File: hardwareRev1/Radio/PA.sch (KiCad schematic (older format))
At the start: 26 parts

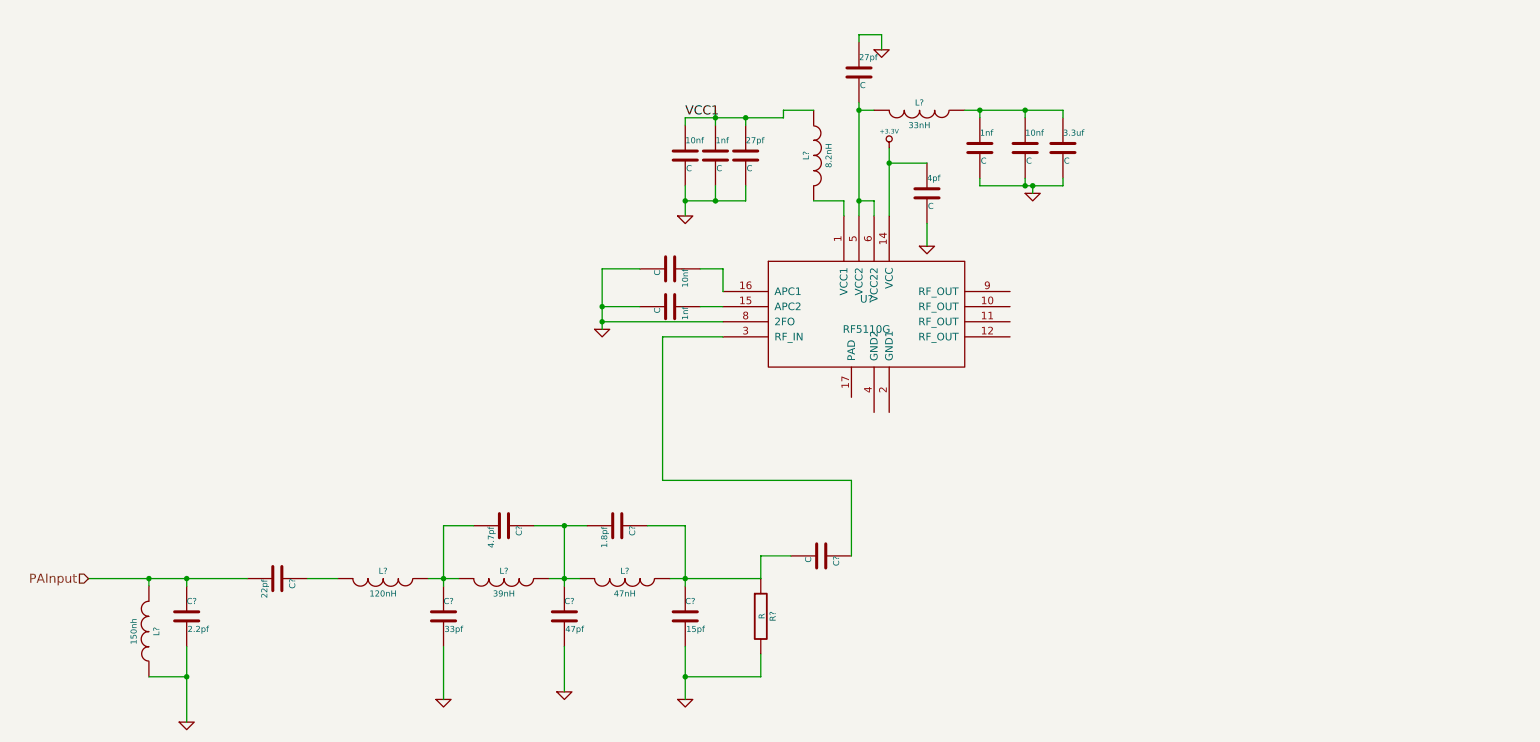
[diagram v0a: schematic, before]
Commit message: Added the outline for the RF module. Also finished the schematic.
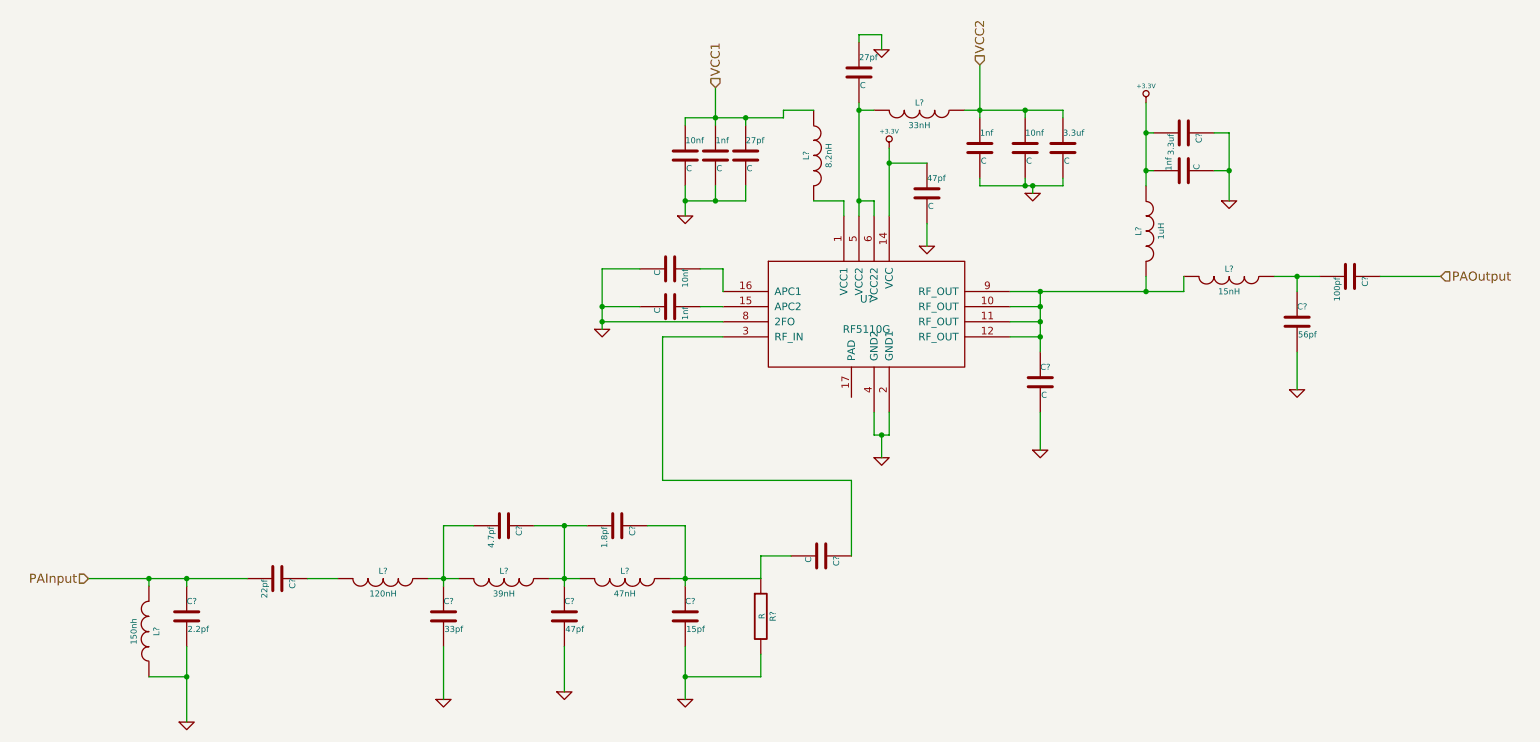
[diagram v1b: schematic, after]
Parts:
- added 1nf, C?: C, symbol C
- added C?: 3.3uf, symbol C
- added C?: 56pf, symbol C
- added C?: 100pf, symbol C
- added L?: 1uH, symbol INDUCTOR
- added L?: 15nH, symbol INDUCTOR
- renumbered 4pf to 47pf
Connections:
- net +3.3V: now also 1nf.1, C?.2, L?.1
- net GND: now also U?.2 (GND1), U?.4 (GND2), 1nf.2, C?.1, C?.2, C?.2
- net at U?.10 (RF_OUT): now also U?.11 (RF_OUT), U?.12 (RF_OUT), U?.9 (RF_OUT), C?.1, L?.2, L?.2
- net VCC2: now reaches 10nf.1, 1nf.1, 3.3uf.1, L?.1
- new net: C?.1, C?.2, L?.1
- new net PAOutput: C?.1

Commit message: added the radio .
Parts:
- C11, C12, C13, C14, C15, C16, C20, C23, C28, C32, C33: renamed from C?; footprint (none) -> Capacitors_SMD:C_0402
- C17, C19, C27: renamed from 10nf; value C -> 10nf; footprint (none) -> Capacitors_SMD:C_0402
- C18, C21, C26, C31: renamed from 1nf; value C -> 1nf; footprint (none) -> Capacitors_SMD:C_0402
- C22, C24: renamed from 27pf; value C -> 27pf; footprint (none) -> Capacitors_SMD:C_0402
- C25: renamed from 47pf; value C -> 47pf; footprint (none) -> Capacitors_SMD:C_0402
- C29: renamed from 3.3uf; value C -> 3.3uf; footprint (none) -> Capacitors_SMD:C_1206
- C30: renamed from C?; footprint (none) -> Capacitors_SMD:C_1206
- L10, L11, L12, L14, L15, L8, L9: renamed from L?; footprint (none) -> Resistors_SMD:R_0402
- L13: renamed from L?; footprint (none) -> Resistors_SMD:R_1206
- R1: renamed from R?; footprint (none) -> Resistors_SMD:R_0402
- U3: renamed from U?; footprint MODULE -> w_smd_qfn:qfn-16
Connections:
- net GND: now also U3.17 (PAD)

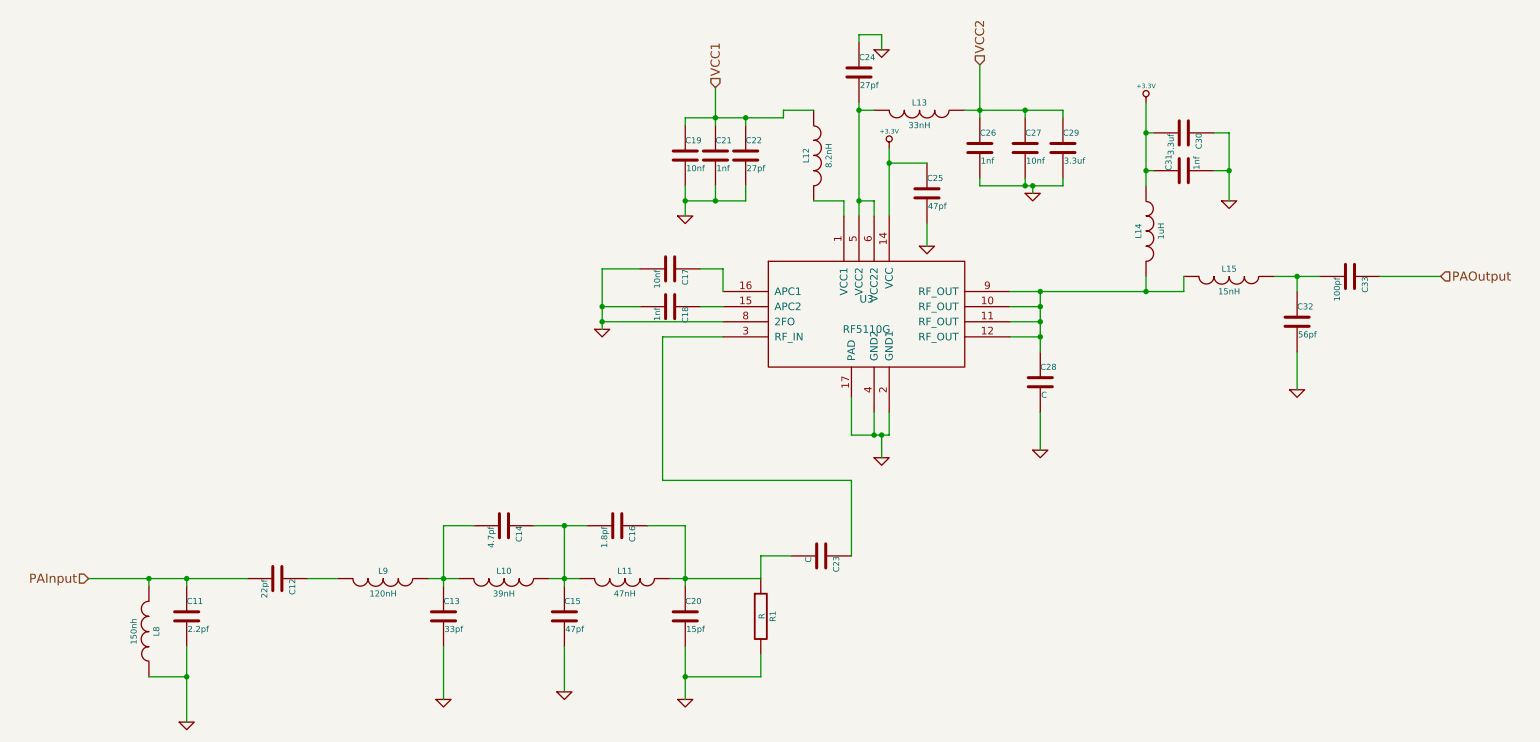
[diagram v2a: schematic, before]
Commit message: Finished the PCB for the new radio module.
Still needs to be checked.
Added the datasheet for the amp and switch
Added the footprint for a 1.27mm pitch 2X8 connector
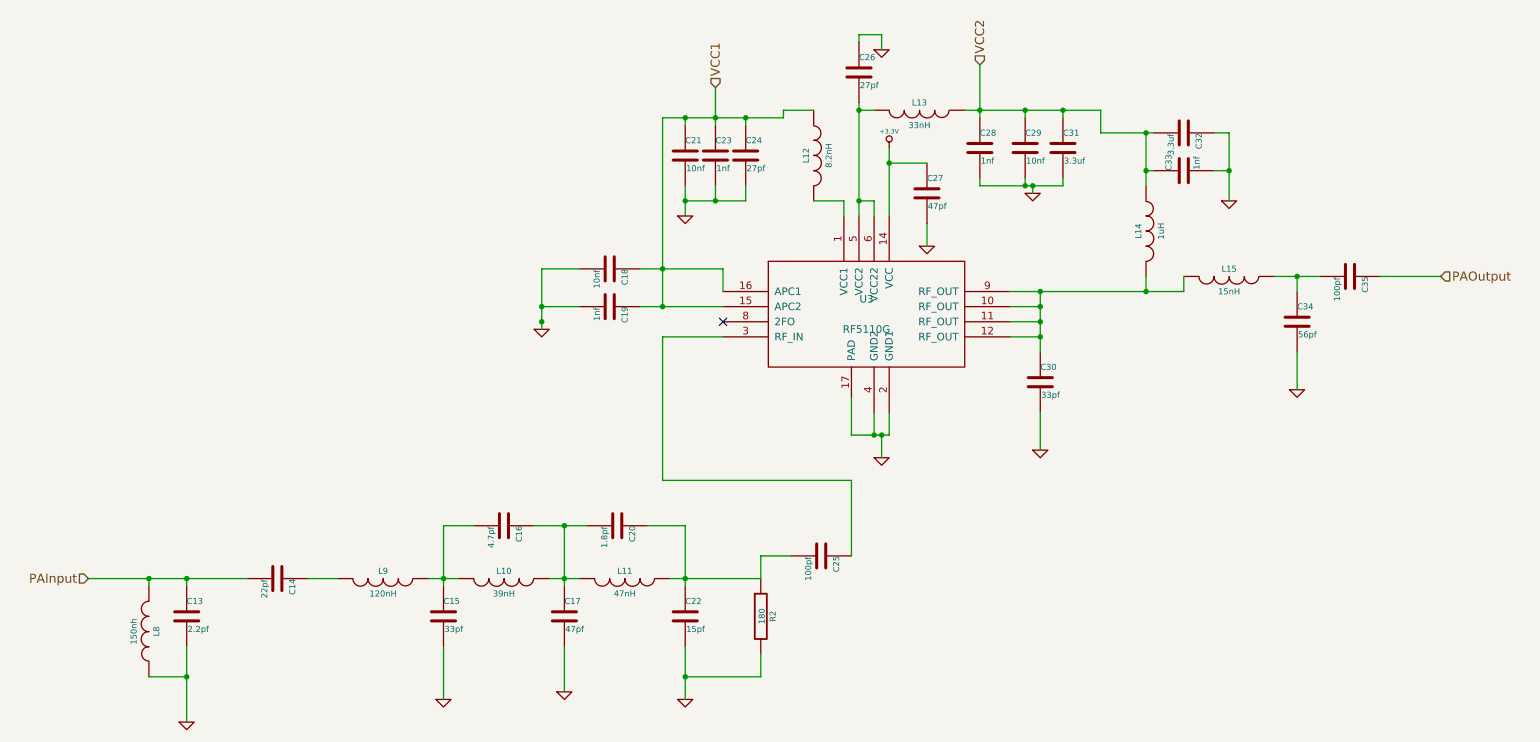
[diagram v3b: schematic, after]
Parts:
- C25: renamed from C23; value C -> 100pf
- C30: renamed from C28; value C -> 33pf
- R2: renamed from R1; value R -> 180
- U3: footprint w_smd_qfn:qfn-16 -> Housings_DFN_QFN:QFN-16-1EP_3x3mm_Pitch0.5mm
- renumbered C11 to C13, C12 to C14, C13 to C15, C14 to C16, C15 to C17, C17 to C18, C18 to C19, C16 to C20, C19 to C21, C20 to C22, C21 to C23, C22 to C24, C24 to C26, C25 to C27, C26 to C28, C27 to C29, C29 to C31, C30 to C32, C31 to C33, C32 to C34, C33 to C35
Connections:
- net +3.3V: no longer C32.2, C33.1, L14.1
- net GND: no longer U3.8 (2FO)
- net VCC1: now also C18.1, C19.1, U3.15 (APC2), U3.16 (APC1)
- net VCC2: now also C32.2, C33.1, L14.1
- no-connect marks 0 -> 1
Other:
- moved on the sheet: C18, C19

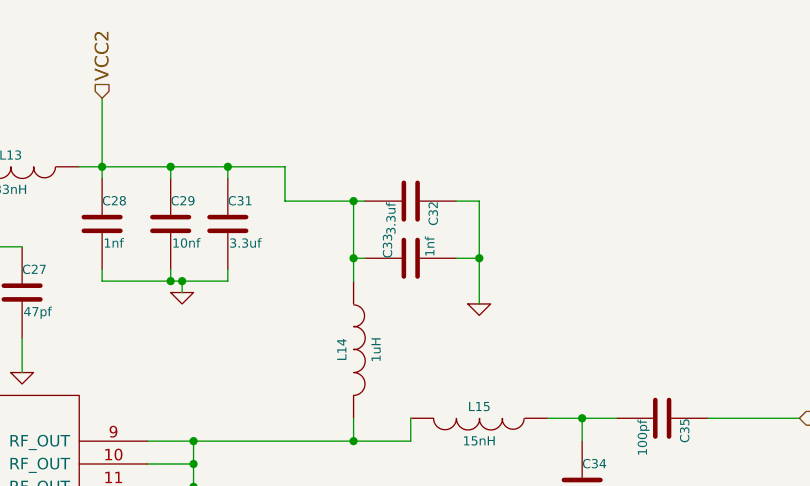
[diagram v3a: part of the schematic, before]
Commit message: Added a capacitor to the power amp sheet in order to facilitate 440.
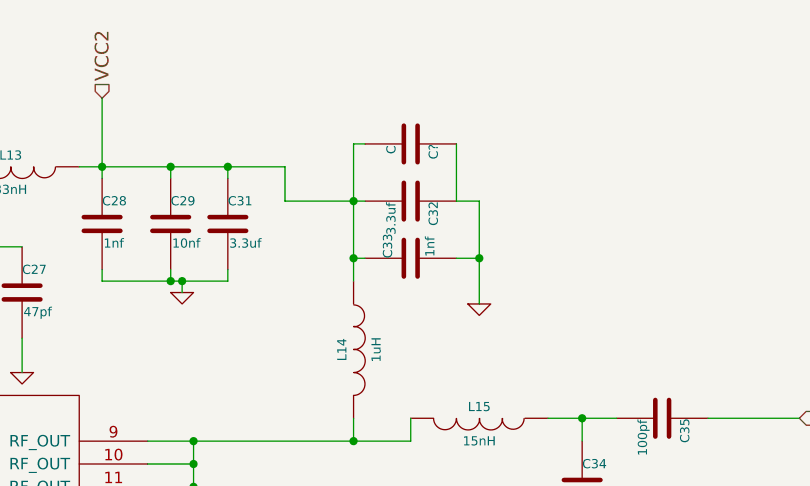
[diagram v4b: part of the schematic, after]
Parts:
- added C?: C, symbol C
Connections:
- net GND: now also C?.1
- net VCC2: now also C?.2
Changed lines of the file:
@@
 Connection ~ 7450 2850
 Wire Wire Line
-	8000 3000 8000 3350
+	8000 2750 8000 3350
 NoConn ~ 5200 4250
+$Comp
+L C C?
+U 1 1 55F187F6
+P 8250 2750
+F 0 "C?" H 8250 2850 40  0000 L CNN
+F 1 "C" H 8256 2665 40  0000 L CNN
+F 2 "" H 8288 2600 30  0000 C CNN
+F 3 "" H 8250 2750 60  0000 C CNN
+	1    8250 2750
+	0    1    1    0
+$EndComp
+Wire Wire Line
+	8000 2750 8050 2750
+Wire Wire Line
+	8450 2750 8450 3000
 $EndSCHEMATC

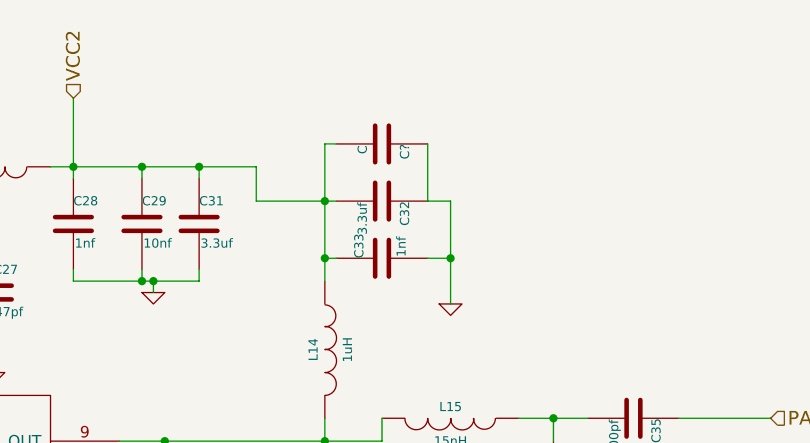
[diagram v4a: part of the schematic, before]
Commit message: Rerouted some power traces. Need to rerout it again.
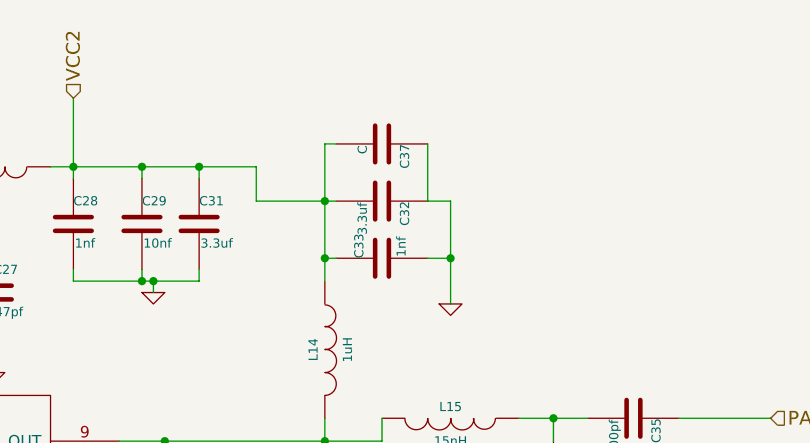
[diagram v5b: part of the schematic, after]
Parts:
- gave numbers to parts that had none: 1
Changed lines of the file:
@@
 $EndComp
 $Comp
-L GND #PWR025
+L GND #PWR25
 U 1 1 55503EBE
 P 1650 6900
-F 0 "#PWR025" H 1650 6900 30  0001 C CNN
+F 0 "#PWR25" H 1650 6900 30  0001 C CNN
 F 1 "GND" H 1650 6830 30  0001 C CNN
 F 2 "" H 1650 6900 60  0000 C CNN
@@
 $EndComp
 $Comp
-L GND #PWR026
+L GND #PWR26
 U 1 1 55503EDE
 P 3350 6750
-F 0 "#PWR026" H 3350 6750 30  0001 C CNN
+F 0 "#PWR26" H 3350 6750 30  0001 C CNN
 F 1 "GND" H 3350 6680 30  0001 C CNN
 F 2 "" H 3350 6750 60  0000 C CNN
@@
 $EndComp
 $Comp
-L GND #PWR027
+L GND #PWR28
 U 1 1 55503EFE
 P 4150 6700
-F 0 "#PWR027" H 4150 6700 30  0001 C CNN
+F 0 "#PWR28" H 4150 6700 30  0001 C CNN
 F 1 "GND" H 4150 6630 30  0001 C CNN
 F 2 "" H 4150 6700 60  0000 C CNN
@@
 $EndComp
 $Comp
-L GND #PWR028
+L GND #PWR30
 U 1 1 55503F1E
 P 4950 6750
-F 0 "#PWR028" H 4950 6750 30  0001 C CNN
+F 0 "#PWR30" H 4950 6750 30  0001 C CNN
 F 1 "GND" H 4950 6680 30  0001 C CNN
 F 2 "" H 4950 6750 60  0000 C CNN
@@
 $EndComp
 $Comp
-L GND #PWR029
+L GND #PWR29
 U 1 1 55508EF7
 P 4950 3550
-F 0 "#PWR029" H 4950 3550 30  0001 C CNN
+F 0 "#PWR29" H 4950 3550 30  0001 C CNN
 F 1 "GND" H 4950 3480 30  0001 C CNN
 F 2 "" H 4950 3550 60  0000 C CNN
@@
 $EndComp
 $Comp
-L GND #PWR030
+L GND #PWR35
 U 1 1 5550A22C
 P 7250 3400
-F 0 "#PWR030" H 7250 3400 30  0001 C CNN
+F 0 "#PWR35" H 7250 3400 30  0001 C CNN
 F 1 "GND" H 7250 3330 30  0001 C CNN
 F 2 "" H 7250 3400 60  0000 C CNN
@@
 $EndComp
 $Comp
-L GND #PWR031
+L GND #PWR31
 U 1 1 5550A374
 P 6250 2450
-F 0 "#PWR031" H 6250 2450 30  0001 C CNN
+F 0 "#PWR31" H 6250 2450 30  0001 C CNN
 F 1 "GND" H 6250 2380 30  0001 C CNN
 F 2 "" H 6250 2450 60  0000 C CNN
@@
 $EndComp
 $Comp
-L GND #PWR032
+L GND #PWR34
 U 1 1 5550B4DF
 P 6550 3750
-F 0 "#PWR032" H 6550 3750 30  0001 C CNN
+F 0 "#PWR34" H 6550 3750 30  0001 C CNN
 F 1 "GND" H 6550 3680 30  0001 C CNN
 F 2 "" H 6550 3750 60  0000 C CNN
@@
 $EndComp
 $Comp
-L +3.3V #PWR033
+L +3.3V #PWR33
 U 1 1 5550B51F
 P 6300 3100
-F 0 "#PWR033" H 6300 3060 30  0001 C CNN
+F 0 "#PWR33" H 6300 3060 30  0001 C CNN
 F 1 "+3.3V" H 6300 3210 30  0000 C CNN
 F 2 "" H 6300 3100 60  0000 C CNN
@@
 $EndComp
 $Comp
-L GND #PWR034
+L GND #PWR27
 U 1 1 5550B9EE
 P 4000 4300
-F 0 "#PWR034" H 4000 4300 30  0001 C CNN
+F 0 "#PWR27" H 4000 4300 30  0001 C CNN
 F 1 "GND" H 4000 4230 30  0001 C CNN
 F 2 "" H 4000 4300 60  0000 C CNN
@@
 $EndComp
 $Comp
-L GND #PWR035
+L GND #PWR36
 U 1 1 5550EACC
 P 7300 5100
-F 0 "#PWR035" H 7300 5100 30  0001 C CNN
+F 0 "#PWR36" H 7300 5100 30  0001 C CNN
 F 1 "GND" H 7300 5030 30  0001 C CNN
 F 2 "" H 7300 5100 60  0000 C CNN
@@
 $EndComp
 $Comp
-L GND #PWR036
+L GND #PWR38
 U 1 1 5550EB01
 P 9000 4700
-F 0 "#PWR036" H 9000 4700 30  0001 C CNN
+F 0 "#PWR38" H 9000 4700 30  0001 C CNN
 F 1 "GND" H 9000 4630 30  0001 C CNN
 F 2 "" H 9000 4700 60  0000 C CNN
@@
 $EndComp
 $Comp
-L GND #PWR037
+L GND #PWR37
 U 1 1 5550EB36
 P 8550 3450
-F 0 "#PWR037" H 8550 3450 30  0001 C CNN
+F 0 "#PWR37" H 8550 3450 30  0001 C CNN
 F 1 "GND" H 8550 3380 30  0001 C CNN
 F 2 "" H 8550 3450 60  0000 C CNN
@@
 $EndComp
 $Comp
-L GND #PWR038
+L GND #PWR32
 U 1 1 5550EB6B
 P 6250 5150
-F 0 "#PWR038" H 6250 5150 30  0001 C CNN
+F 0 "#PWR32" H 6250 5150 30  0001 C CNN
 F 1 "GND" H 6250 5080 30  0001 C CNN
 F 2 "" H 6250 5150 60  0000 C CNN
@@
 NoConn ~ 5200 4250
 $Comp
-L C C?
+L C C37
 U 1 1 55F187F6
 P 8250 2750
-F 0 "C?" H 8250 2850 40  0000 L CNN
+F 0 "C37" H 8250 2850 40  0000 L CNN
 F 1 "C" H 8256 2665 40  0000 L CNN
 F 2 "" H 8288 2600 30  0000 C CNN
